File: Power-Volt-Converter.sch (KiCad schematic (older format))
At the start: 29 parts, among them P22 XT60, P23 XT60, P24 XT60, P25 XT60, P26 XT60, P27 XT60, P28 XT60, P29 XT60, Q15 BC817-40, U10 TEN_20-2411WIN, U11 TEN_20-2411WIN, U7 UWE-12/6-Q12P, U8 UWE-12/6-Q12P, U9 UWE-12/6-Q12P

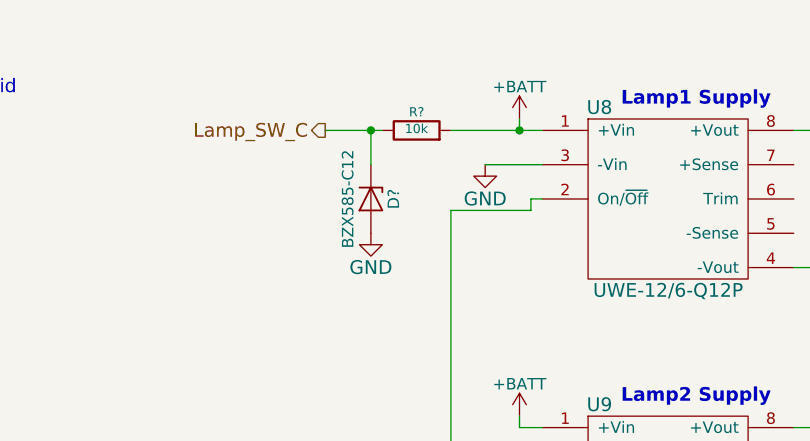
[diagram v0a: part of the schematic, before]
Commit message: update footprint of JP1
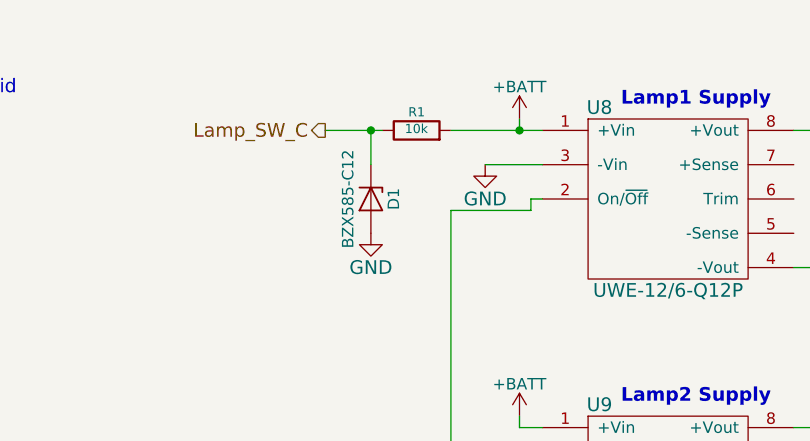
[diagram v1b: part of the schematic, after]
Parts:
- JP1: footprint Pin_Headers:Pin_Header_Straight_1x02 -> Pin_Headers:Pin_Header_Straight_1x02_Pitch2.00mm
- gave numbers to parts that had none: 2
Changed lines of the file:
@@
 LIBS:zeabus
 LIBS:ftdi
+LIBS:Power_Distributor-cache
 EELAYER 25 0
 EELAYER END
@@
 $EndDescr
 $Comp
-L GND #PWR050
+L GND #PWR53
 U 1 1 58C84F3D
 P 7650 1850
-F 0 "#PWR050" H 7650 1600 60  0001 C CNN
+F 0 "#PWR53" H 7650 1600 60  0001 C CNN
 F 1 "GND" H 7650 1700 60  0000 C CNN
 F 2 "" H 7650 1850 60  0000 C CNN
@@
 	9000 2300 9600 2300
 $Comp
-L GND #PWR051
+L GND #PWR47
 U 1 1 58C8506B
 P 2250 1600
-F 0 "#PWR051" H 2250 1350 60  0001 C CNN
+F 0 "#PWR47" H 2250 1350 60  0001 C CNN
 F 1 "GND" H 2250 1450 60  0000 C CNN
 F 2 "" H 2250 1600 60  0000 C CNN
@@
 $EndComp
 $Comp
-L GND #PWR052
+L GND #PWR50
 U 1 1 58C8524E
 P 2500 3900
-F 0 "#PWR052" H 2500 3650 60  0001 C CNN
+F 0 "#PWR50" H 2500 3650 60  0001 C CNN
 F 1 "GND" H 2500 3750 60  0000 C CNN
 F 2 "" H 2500 3900 60  0000 C CNN
@@
 +VBatt
 $Comp
-L +BATT #PWR053
+L +BATT #PWR48
 U 1 1 58C81568
 P 2500 1400
-F 0 "#PWR053" H 2500 1250 50  0001 C CNN
+F 0 "#PWR48" H 2500 1250 50  0001 C CNN
 F 1 "+BATT" H 2500 1540 50  0000 C CNN
 F 2 "" H 2500 1400 50  0000 C CNN
@@
 F 0 "JP1" H 1850 2650 50  0000 C CNN
 F 1 "Main Switch (N.O.)" H 1850 2420 50  0000 C CNN
-F 2 "Pin_Headers:Pin_Header_Straight_1x02" H 1850 2500 60  0001 C CNN
+F 2 "Pin_Headers:Pin_Header_Straight_1x02_Pitch2.00mm" H 1850 2500 60  0001 C CNN
 F 3 "" H 1850 2500 60  0000 C CNN
 	1    1850 2500
@@
 $EndComp
 $Comp
-L GND #PWR054
+L GND #PWR51
 U 1 1 58C8A79D
 P 2600 2700
-F 0 "#PWR054" H 2600 2450 60  0001 C CNN
+F 0 "#PWR51" H 2600 2450 60  0001 C CNN
 F 1 "GND" H 2600 2550 60  0000 C CNN
 F 2 "" H 2600 2700 60  0000 C CNN
@@
 	2250 2050 2250 2150
 $Comp
-L GND #PWR055
+L GND #PWR46
 U 1 1 58C8B273
 P 1450 2700
-F 0 "#PWR055" H 1450 2450 60  0001 C CNN
+F 0 "#PWR46" H 1450 2450 60  0001 C CNN
 F 1 "GND" H 1450 2550 60  0000 C CNN
 F 2 "" H 1450 2700 60  0000 C CNN
@@
 Connection ~ 2000 1450
 $Comp
-L +BATT #PWR056
+L +BATT #PWR49
 U 1 1 58C8C536
 P 2500 3550
-F 0 "#PWR056" H 2500 3400 50  0001 C CNN
+F 0 "#PWR49" H 2500 3400 50  0001 C CNN
 F 1 "+BATT" H 2500 3690 50  0000 C CNN
 F 2 "" H 2500 3550 50  0000 C CNN
@@
 	7850 2000 7900 2000
 $Comp
-L +BATT #PWR057
+L +BATT #PWR57
 U 1 1 58C8D087
 P 7800 1650
-F 0 "#PWR057" H 7800 1500 50  0001 C CNN
+F 0 "#PWR57" H 7800 1500 50  0001 C CNN
 F 1 "+BATT" H 7800 1790 50  0000 C CNN
 F 2 "" H 7800 1650 50  0000 C CNN
@@
 Lamp1
 $Comp
-L GND #PWR058
+L GND #PWR54
 U 1 1 58C8E084
 P 7650 3150
-F 0 "#PWR058" H 7650 2900 60  0001 C CNN
+F 0 "#PWR54" H 7650 2900 60  0001 C CNN
 F 1 "GND" H 7650 3000 60  0000 C CNN
 F 2 "" H 7650 3150 60  0000 C CNN
@@
 Lamp_SW_E
 $Comp
-L GND #PWR059
+L GND #PWR60
 U 1 1 58C8E0B5
 P 7850 3750
-F 0 "#PWR059" H 7850 3500 60  0001 C CNN
+F 0 "#PWR60" H 7850 3500 60  0001 C CNN
 F 1 "GND" H 7850 3600 60  0000 C CNN
 F 2 "" H 7850 3750 60  0000 C CNN
@@
 Connection ~ 7850 3400
 $Comp
-L +BATT #PWR060
+L +BATT #PWR58
 U 1 1 58C8E0C7
 P 7800 2950
-F 0 "#PWR060" H 7800 2800 50  0001 C CNN
+F 0 "#PWR58" H 7800 2800 50  0001 C CNN
 F 1 "+BATT" H 7800 3090 50  0000 C CNN
 F 2 "" H 7800 2950 50  0000 C CNN
@@
 $EndComp
 $Comp
-L GND #PWR061
+L GND #PWR56
 U 1 1 58C9097C
 P 7700 5400
-F 0 "#PWR061" H 7700 5150 60  0001 C CNN
+F 0 "#PWR56" H 7700 5150 60  0001 C CNN
 F 1 "GND" H 7700 5250 60  0000 C CNN
 F 2 "" H 7700 5400 60  0000 C CNN
@@
 	7800 5400 7800 5700
 $Comp
-L +BATT #PWR062
+L +BATT #PWR55
 U 1 1 58C909A2
 P 7700 5050
-F 0 "#PWR062" H 7700 4900 50  0001 C CNN
+F 0 "#PWR55" H 7700 4900 50  0001 C CNN
 F 1 "+BATT" H 7700 5190 50  0000 C CNN
 F 2 "" H 7700 5050 50  0000 C CNN
@@
 $EndComp
 $Comp
-L GND #PWR063
+L GND #PWR59
 U 1 1 58C909A9
 P 7800 6000
-F 0 "#PWR063" H 7800 5750 60  0001 C CNN
+F 0 "#PWR59" H 7800 5750 60  0001 C CNN
 F 1 "GND" H 7800 5850 60  0000 C CNN
 F 2 "" H 7800 6000 60  0000 C CNN
@@
 Connection ~ 2600 2250
 $Comp
-L D_Zener D?
+L D_Zener D1
 U 1 1 58E6F6E6
 P 7150 2000
-F 0 "D?" H 7150 2100 50  0000 C CNN
+F 0 "D1" H 7150 2100 50  0000 C CNN
 F 1 "BZX585-C12" H 7150 1900 50  0000 C CNN
 F 2 "Diodes_SMD:D_SOD-523" H 7150 2000 50  0001 C CNN
@@
 $EndComp
 $Comp
-L R R?
+L R R1
 U 1 1 58E6F94F
 P 7350 1700
-F 0 "R?" V 7430 1700 40  0000 C CNN
+F 0 "R1" V 7430 1700 40  0000 C CNN
 F 1 "10k" V 7357 1701 40  0000 C CNN
 F 2 "Resistors_SMD:R_0603" V 7280 1700 30  0001 C CNN
@@
 Connection ~ 7150 1700
 $Comp
-L GND #PWR064
+L GND #PWR52
 U 1 1 58E6FD35
 P 7150 2150
-F 0 "#PWR064" H 7150 1900 60  0001 C CNN
+F 0 "#PWR52" H 7150 1900 60  0001 C CNN
 F 1 "GND" H 7150 2000 60  0000 C CNN
 F 2 "" H 7150 2150 60  0000 C CNN

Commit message: update footprint of some LED
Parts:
- D17, D18, D19, D20, D21: footprint LEDs:LED-0603 -> LEDs:LED_0603
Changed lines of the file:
@@
 $EndDescr
 $Comp
-L GND #PWR53
+L GND #PWR046
 U 1 1 58C84F3D
 P 7650 1850
-F 0 "#PWR53" H 7650 1600 60  0001 C CNN
+F 0 "#PWR046" H 7650 1600 60  0001 C CNN
 F 1 "GND" H 7650 1700 60  0000 C CNN
 F 2 "" H 7650 1850 60  0000 C CNN
@@
 F 0 "D18" H 9250 2275 50  0000 L CNN
 F 1 "Led_Small" H 9125 2050 50  0000 L CNN
-F 2 "LEDs:LED-0603" V 9300 2150 60  0001 C CNN
+F 2 "LEDs:LED_0603" V 9300 2150 60  0001 C CNN
 F 3 "" V 9300 2150 60  0000 C CNN
 	1    9300 2150
@@
 	9000 2300 9600 2300
 $Comp
-L GND #PWR47
+L GND #PWR047
 U 1 1 58C8506B
 P 2250 1600
-F 0 "#PWR47" H 2250 1350 60  0001 C CNN
+F 0 "#PWR047" H 2250 1350 60  0001 C CNN
 F 1 "GND" H 2250 1450 60  0000 C CNN
 F 2 "" H 2250 1600 60  0000 C CNN
@@
 F 0 "D17" H 3950 2025 50  0000 L CNN
 F 1 "Led_Small" H 3825 1800 50  0000 L CNN
-F 2 "LEDs:LED-0603" V 4000 1900 60  0001 C CNN
+F 2 "LEDs:LED_0603" V 4000 1900 60  0001 C CNN
 F 3 "" V 4000 1900 60  0000 C CNN
 	1    4000 1900
@@
 F 0 "D20" H 4150 4175 50  0000 L CNN
 F 1 "Led_Small" H 4025 3950 50  0000 L CNN
-F 2 "LEDs:LED-0603" V 4200 4050 60  0001 C CNN
+F 2 "LEDs:LED_0603" V 4200 4050 60  0001 C CNN
 F 3 "" V 4200 4050 60  0000 C CNN
 	1    4200 4050
@@
 $EndComp
 $Comp
-L GND #PWR50
+L GND #PWR048
 U 1 1 58C8524E
 P 2500 3900
-F 0 "#PWR50" H 2500 3650 60  0001 C CNN
+F 0 "#PWR048" H 2500 3650 60  0001 C CNN
 F 1 "GND" H 2500 3750 60  0000 C CNN
 F 2 "" H 2500 3900 60  0000 C CNN
@@
 +VBatt
 $Comp
-L +BATT #PWR48
+L +BATT #PWR049
 U 1 1 58C81568
 P 2500 1400
-F 0 "#PWR48" H 2500 1250 50  0001 C CNN
+F 0 "#PWR049" H 2500 1250 50  0001 C CNN
 F 1 "+BATT" H 2500 1540 50  0000 C CNN
 F 2 "" H 2500 1400 50  0000 C CNN
@@
 $EndComp
 $Comp
-L GND #PWR51
+L GND #PWR050
 U 1 1 58C8A79D
 P 2600 2700
-F 0 "#PWR51" H 2600 2450 60  0001 C CNN
+F 0 "#PWR050" H 2600 2450 60  0001 C CNN
 F 1 "GND" H 2600 2550 60  0000 C CNN
 F 2 "" H 2600 2700 60  0000 C CNN
@@
 	2250 2050 2250 2150
 $Comp
-L GND #PWR46
+L GND #PWR051
 U 1 1 58C8B273
 P 1450 2700
-F 0 "#PWR46" H 1450 2450 60  0001 C CNN
+F 0 "#PWR051" H 1450 2450 60  0001 C CNN
 F 1 "GND" H 1450 2550 60  0000 C CNN
 F 2 "" H 1450 2700 60  0000 C CNN
@@
 Connection ~ 2000 1450
 $Comp
-L +BATT #PWR49
+L +BATT #PWR052
 U 1 1 58C8C536
 P 2500 3550
-F 0 "#PWR49" H 2500 3400 50  0001 C CNN
+F 0 "#PWR052" H 2500 3400 50  0001 C CNN
 F 1 "+BATT" H 2500 3690 50  0000 C CNN
 F 2 "" H 2500 3550 50  0000 C CNN
@@
 	7850 2000 7900 2000
 $Comp
-L +BATT #PWR57
+L +BATT #PWR053
 U 1 1 58C8D087
 P 7800 1650
-F 0 "#PWR57" H 7800 1500 50  0001 C CNN
+F 0 "#PWR053" H 7800 1500 50  0001 C CNN
 F 1 "+BATT" H 7800 1790 50  0000 C CNN
 F 2 "" H 7800 1650 50  0000 C CNN
@@
 Lamp1
 $Comp
-L GND #PWR54
+L GND #PWR054
 U 1 1 58C8E084
 P 7650 3150
-F 0 "#PWR54" H 7650 2900 60  0001 C CNN
+F 0 "#PWR054" H 7650 2900 60  0001 C CNN
 F 1 "GND" H 7650 3000 60  0000 C CNN
 F 2 "" H 7650 3150 60  0000 C CNN
@@
 F 0 "D19" H 9250 3575 50  0000 L CNN
 F 1 "Led_Small" H 9125 3350 50  0000 L CNN
-F 2 "LEDs:LED-0603" V 9300 3450 60  0001 C CNN
+F 2 "LEDs:LED_0603" V 9300 3450 60  0001 C CNN
 F 3 "" V 9300 3450 60  0000 C CNN
 	1    9300 3450
@@
 Lamp_SW_E
 $Comp
-L GND #PWR60
+L GND #PWR055
 U 1 1 58C8E0B5
 P 7850 3750
-F 0 "#PWR60" H 7850 3500 60  0001 C CNN
+F 0 "#PWR055" H 7850 3500 60  0001 C CNN
 F 1 "GND" H 7850 3600 60  0000 C CNN
 F 2 "" H 7850 3750 60  0000 C CNN
@@
 Connection ~ 7850 3400
 $Comp
-L +BATT #PWR58
+L +BATT #PWR056
 U 1 1 58C8E0C7
 P 7800 2950
-F 0 "#PWR58" H 7800 2800 50  0001 C CNN
+F 0 "#PWR056" H 7800 2800 50  0001 C CNN
 F 1 "+BATT" H 7800 3090 50  0000 C CNN
 F 2 "" H 7800 2950 50  0000 C CNN
@@
 F 0 "D21" H 9350 5675 50  0000 L CNN
 F 1 "Led_Small" H 9225 5450 50  0000 L CNN
-F 2 "LEDs:LED-0603" V 9400 5550 60  0001 C CNN
+F 2 "LEDs:LED_0603" V 9400 5550 60  0001 C CNN
 F 3 "" V 9400 5550 60  0000 C CNN
 	1    9400 5550
@@
 $EndComp
 $Comp
-L GND #PWR56
+L GND #PWR057
 U 1 1 58C9097C
 P 7700 5400
-F 0 "#PWR56" H 7700 5150 60  0001 C CNN
+F 0 "#PWR057" H 7700 5150 60  0001 C CNN
 F 1 "GND" H 7700 5250 60  0000 C CNN
 F 2 "" H 7700 5400 60  0000 C CNN
@@
 	7800 5400 7800 5700
 $Comp
-L +BATT #PWR55
+L +BATT #PWR058
 U 1 1 58C909A2
 P 7700 5050
-F 0 "#PWR55" H 7700 4900 50  0001 C CNN
+F 0 "#PWR058" H 7700 4900 50  0001 C CNN
 F 1 "+BATT" H 7700 5190 50  0000 C CNN
 F 2 "" H 7700 5050 50  0000 C CNN
@@
 $EndComp
 $Comp
-L GND #PWR59
+L GND #PWR059
 U 1 1 58C909A9
 P 7800 6000
-F 0 "#PWR59" H 7800 5750 60  0001 C CNN
+F 0 "#PWR059" H 7800 5750 60  0001 C CNN
 F 1 "GND" H 7800 5850 60  0000 C CNN
 F 2 "" H 7800 6000 60  0000 C CNN
@@
 Connection ~ 7150 1700
 $Comp
-L GND #PWR52
+L GND #PWR060
 U 1 1 58E6FD35
 P 7150 2150
-F 0 "#PWR52" H 7150 1900 60  0001 C CNN
+F 0 "#PWR060" H 7150 1900 60  0001 C CNN
 F 1 "GND" H 7150 2000 60  0000 C CNN
 F 2 "" H 7150 2150 60  0000 C CNN
